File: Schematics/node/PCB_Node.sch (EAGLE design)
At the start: 19 parts, among them U1 ATMEGA328P, U2 MAX485CSA+, U3 MCP1824ST-3302E/DB

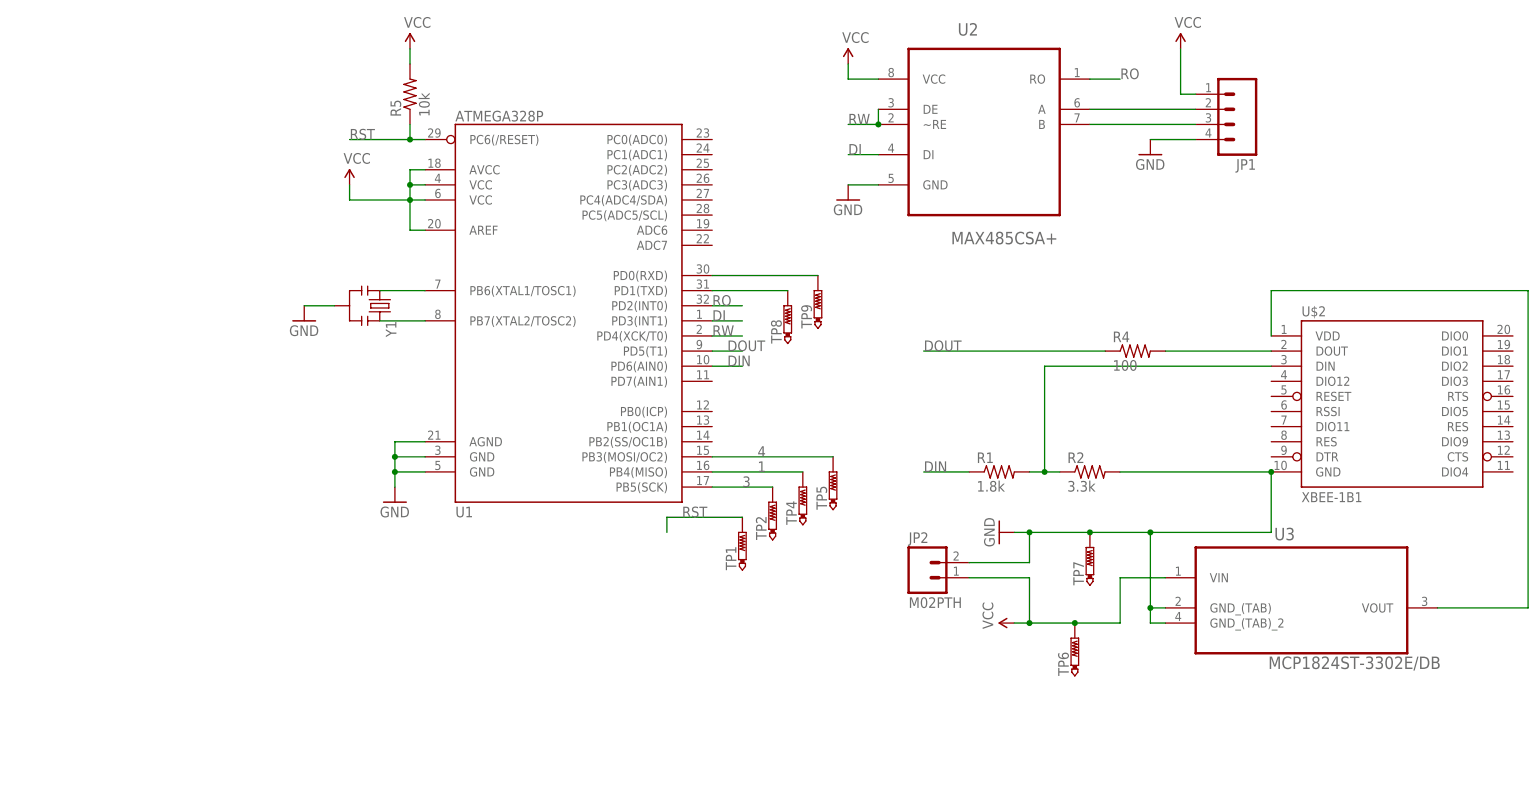
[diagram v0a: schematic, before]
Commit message: PCB updates
changed sensor PCB to 3.0
changed Node PCB to 2.0 and parts list to go with it (Sach, can you
look over the schematic, board, and parts list that I have so far to
make sure I have everything correct?)
added Base Station PCB 0.5
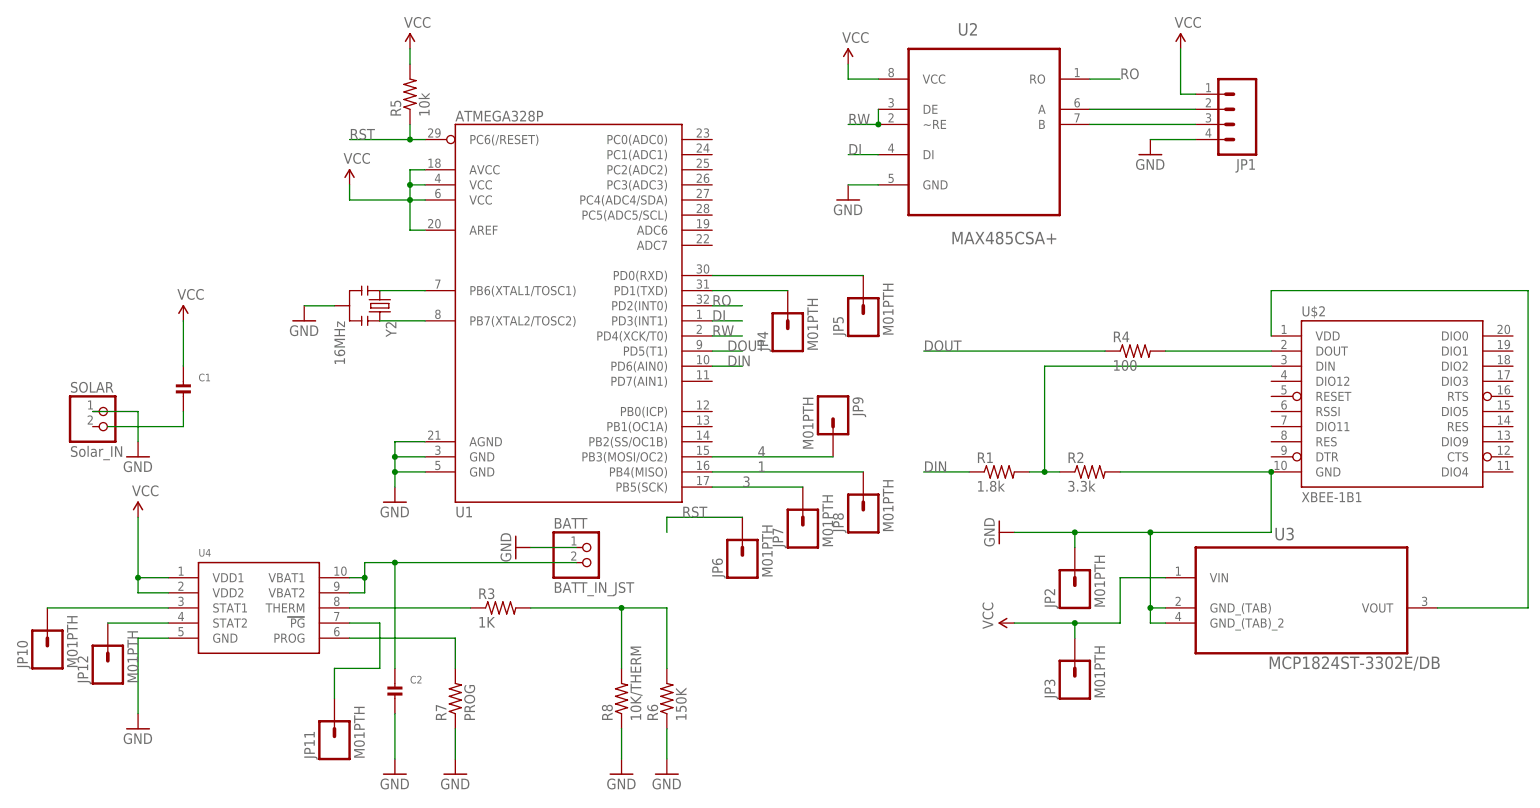
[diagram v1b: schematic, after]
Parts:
- removed TP1, TP2, TP4, TP5, TP6, TP7, TP8, TP9: PTR1TP12R, testpad:PTR1TP12R
- removed Y1: (no value), SparkFun-FreqCtrl:RESONATORPTH
- added BATT: BATT_IN_JST, microbuilder:JST_2PIN
- added C1, C2: (no value), microbuilder:CAP_CERAMIC0805
- added JP10, JP11, JP12, JP3, JP4, JP5, JP6, JP7, JP8, JP9: M01PTH, SparkFun-Connectors:M01PTH
- added R3: 1K, adafruit:R-US_R0805
- added R6: 150K, adafruit:R-US_R0805
- added R7: PROG, microbuilder:RESISTOR_DUAL
- added R8: 10K/THERM, adafruit:R-US_FLIPFLOP
- added SOLAR: Solar_IN, microbuilder:JST_2PIN
- added U4: (no value), microbuilder:MCP73833
- added Y2: 16MHz, SparkFun-FreqCtrl:RESONATOR16MHZ
- JP2: value M02PTH -> M01PTH; device SparkFun-Connectors:M02PTH -> SparkFun-Connectors:M01PTH
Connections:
- new net N$10: JP12.1, U4.STAT2
- new net N$11: JP11.1, U4.PG
- new net N$19: BATT.2, C2.P$1, U4.VBAT1, U4.VBAT2
- new net N$3: R7.2, U4.PROG
- new net N$5: R3.1, U4.THERM
- new net N$7: R3.2, R6.2, R8.2
- new net N$8: C1.P$2
- new net N$9: JP10.1, U4.STAT1
- net 1: now also JP8.1; no longer TP4.TP
- net 3: now also JP7.1; no longer TP2.TP
- net 4: now also JP9.1; no longer TP5.TP
- net GND: now also BATT.1, C2.P$2, JP2.1, R6.1, R7.1, R8.1, SOLAR.1, U4.GND, Y2.2; no longer JP2.2, TP7.TP, Y1.2
- net N$12: now also Y2.3; no longer Y1.3
- net N$13: now also Y2.1; no longer Y1.1
- net N$15: now also JP4.1; no longer TP8.TP
- net N$16: now also JP5.1; no longer TP9.TP
- net RST: now also JP6.1; no longer TP1.TP
- net VCC: now also C1.P$1, JP3.1, U4.VDD1, U4.VDD2; no longer JP2.1, TP6.TP

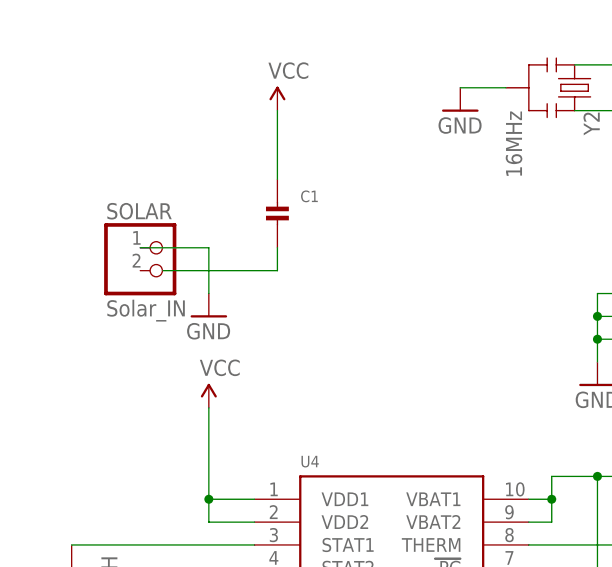
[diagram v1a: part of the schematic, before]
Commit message: Corrected Node PCB issues found by Sachleen for version 2.0
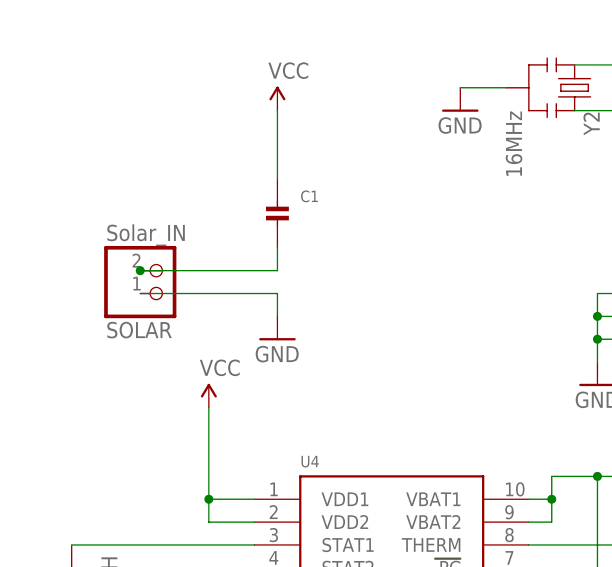
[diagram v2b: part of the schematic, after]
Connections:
- net N$8: now also SOLAR.2
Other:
- moved on the sheet: SOLAR
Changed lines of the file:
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@@
 <instance part="U4" gate="G$1" x="-144.78" y="25.4"/>
 <instance part="BATT" gate="G$1" x="-88.9" y="35.56"/>
-<instance part="SOLAR" gate="G$1" x="-170.18" y="58.42"/>
+<instance part="SOLAR" gate="G$1" x="-170.18" y="58.42" rot="MR180"/>
 <instance part="C1" gate="G$1" x="-157.48" y="63.5"/>
 <instance part="R3" gate="G$1" x="-104.14" y="27.94"/>
@@
 <instance part="GND10" gate="1" x="-76.2" y="0"/>
 <instance part="GND11" gate="1" x="-101.6" y="38.1" rot="R270"/>
-<instance part="GND12" gate="1" x="-165.1" y="53.34"/>
+<instance part="GND12" gate="1" x="-157.48" y="50.8"/>
 <instance part="SUPPLY7" gate="G$1" x="-157.48" y="76.2"/>
 <instance part="Y2" gate="G$1" x="-124.46" y="78.74" rot="R270"/>
@@
 </segment>
 <segment>
-<wire x1="-172.72" y1="60.96" x2="-165.1" y2="60.96" width="0.1524" layer="91"/>
+<wire x1="-172.72" y1="55.88" x2="-157.48" y2="55.88" width="0.1524" layer="91"/>
 <pinref part="SOLAR" gate="G$1" pin="1"/>
 <pinref part="GND12" gate="1" pin="GND"/>
-<wire x1="-165.1" y1="60.96" x2="-165.1" y2="55.88" width="0.1524" layer="91"/>
+<wire x1="-157.48" y1="55.88" x2="-157.48" y2="53.34" width="0.1524" layer="91"/>
 </segment>
 <segment>
@@
 <segment>
 <pinref part="C1" gate="G$1" pin="P$2"/>
-<wire x1="-170.18" y1="58.42" x2="-157.48" y2="58.42" width="0.1524" layer="91"/>
+<wire x1="-170.18" y1="58.42" x2="-172.72" y2="58.42" width="0.1524" layer="91"/>
+<wire x1="-172.72" y1="58.42" x2="-157.48" y2="58.42" width="0.1524" layer="91"/>
 <wire x1="-157.48" y1="58.42" x2="-157.48" y2="60.96" width="0.1524" layer="91"/>
-</segment>
-</net>
+<pinref part="SOLAR" gate="G$1" pin="2"/>
+<junction x="-172.72" y="58.42"/>
+</segment>
+</net>

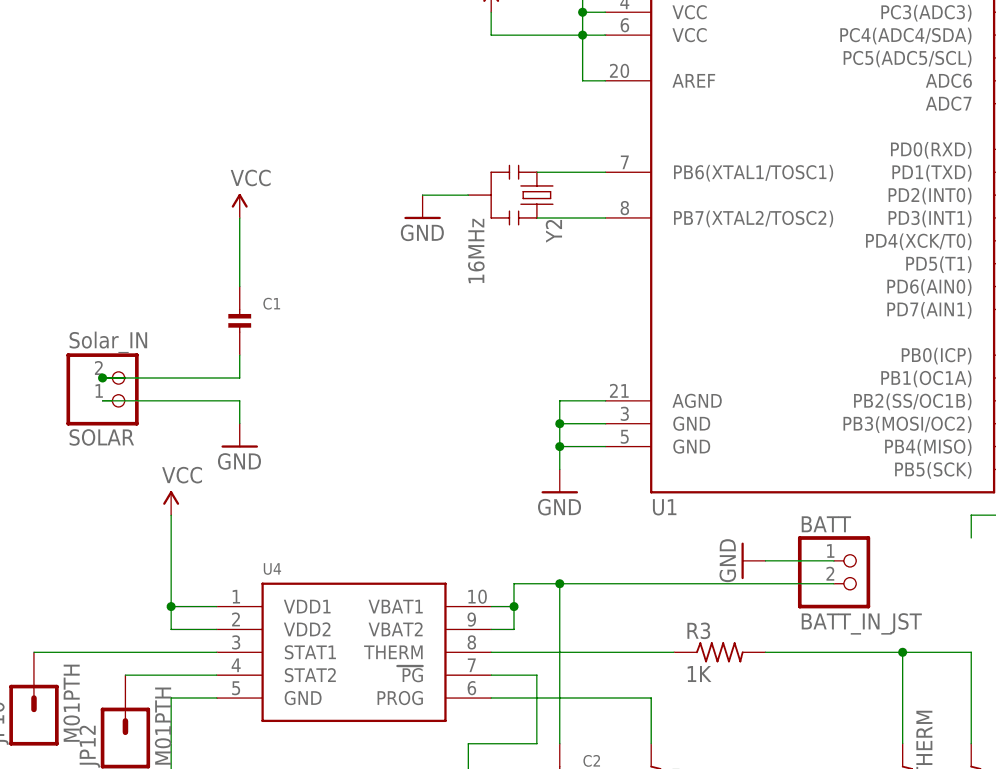
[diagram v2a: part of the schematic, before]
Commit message: Node Fixes
Made fixes to Node PCB.
- connected solar power to charging chip
- made power to battery and atmega from charging chip only
- rearranged board for these changes to work
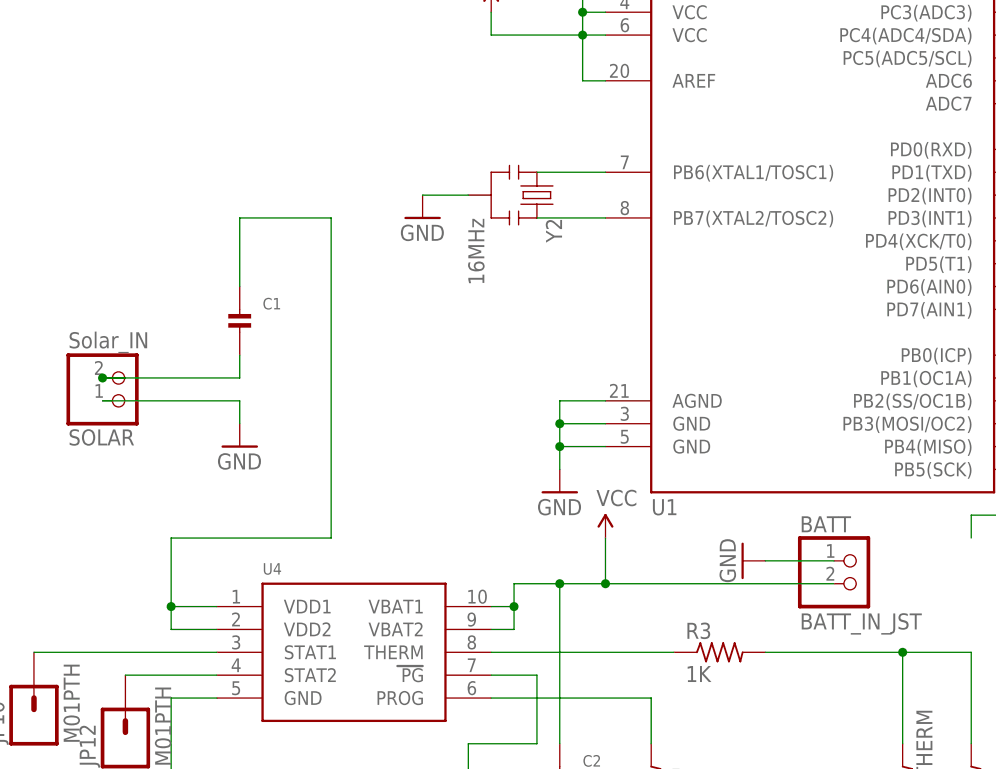
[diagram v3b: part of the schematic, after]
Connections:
- removed net N$19: BATT.2, C2.P$1, U4.VBAT1, U4.VBAT2
- new net N$14: C1.P$1, U4.VDD1, U4.VDD2
- net VCC: now also BATT.2, C2.P$1, U4.VBAT1, U4.VBAT2; no longer C1.P$1, U4.VDD1, U4.VDD2
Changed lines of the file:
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@@
 <part name="R6" library="adafruit" deviceset="R-US_" device="R0805" value="150K"/>
 <part name="R7" library="microbuilder" deviceset="RESISTOR_DUAL" device="" value="PROG"/>
-<part name="SUPPLY5" library="SparkFun-Aesthetics" deviceset="VCC" device=""/>
 <part name="GND6" library="SparkFun-Aesthetics" deviceset="GND" device=""/>
 <part name="R8" library="adafruit" deviceset="R-US_" device="FLIPFLOP" value="10K/THERM"/>
@@
 <part name="GND11" library="SparkFun-Aesthetics" deviceset="GND" device=""/>
 <part name="GND12" library="SparkFun-Aesthetics" deviceset="GND" device=""/>
-<part name="SUPPLY7" library="SparkFun-Aesthetics" deviceset="VCC" device=""/>
 <part name="Y2" library="SparkFun-FreqCtrl" deviceset="RESONATOR" device="16MHZ" value="16MHz"/>
 <part name="JP3" library="SparkFun-Connectors" deviceset="M01" device="PTH"/>
@@
 <part name="JP11" library="SparkFun-Connectors" deviceset="M01" device="PTH"/>
 <part name="JP12" library="SparkFun-Connectors" deviceset="M01" device="PTH"/>
+<part name="SUPPLY5" library="SparkFun-Aesthetics" deviceset="VCC" device=""/>
 </parts>
 <sheets>
@@
 <instance part="R6" gate="G$1" x="-76.2" y="12.7" rot="R90"/>
 <instance part="R7" gate="G$1" x="-111.76" y="12.7" rot="R90"/>
-<instance part="SUPPLY5" gate="G$1" x="-165.1" y="43.18"/>
 <instance part="GND6" gate="1" x="-165.1" y="7.62"/>
 <instance part="R8" gate="G$1" x="-83.82" y="12.7" rot="R90"/>
@@
 <instance part="GND11" gate="1" x="-101.6" y="38.1" rot="R270"/>
 <instance part="GND12" gate="1" x="-157.48" y="50.8"/>
-<instance part="SUPPLY7" gate="G$1" x="-157.48" y="76.2"/>
 <instance part="Y2" gate="G$1" x="-124.46" y="78.74" rot="R270"/>
 <instance part="JP3" gate="G$1" x="-7.62" y="15.24" rot="R90"/>
@@
 <instance part="JP11" gate="G$1" x="-132.08" y="5.08" rot="R90"/>
 <instance part="JP12" gate="G$1" x="-170.18" y="17.78" rot="R90"/>
+<instance part="SUPPLY5" gate="G$1" x="-116.84" y="40.64"/>
 </instances>
 <busses>
@@
 </segment>
 <segment>
-<pinref part="U4" gate="G$1" pin="VDD2"/>
-<pinref part="SUPPLY5" gate="G$1" pin="VCC"/>
-<wire x1="-160.02" y1="30.48" x2="-165.1" y2="30.48" width="0.1524" layer="91"/>
-<wire x1="-165.1" y1="30.48" x2="-165.1" y2="33.02" width="0.1524" layer="91"/>
-<pinref part="U4" gate="G$1" pin="VDD1"/>
-<wire x1="-165.1" y1="33.02" x2="-165.1" y2="43.18" width="0.1524" layer="91"/>
-<wire x1="-160.02" y1="33.02" x2="-165.1" y2="33.02" width="0.1524" layer="91"/>
-<junction x="-165.1" y="33.02"/>
-</segment>
-<segment>
-<pinref part="C1" gate="G$1" pin="P$1"/>
-<pinref part="SUPPLY7" gate="G$1" pin="VCC"/>
-<wire x1="-157.48" y1="68.58" x2="-157.48" y2="76.2" width="0.1524" layer="91"/>
-</segment>
-</net>
-<net name="N$3" class="0">
-<segment>
-<pinref part="U4" gate="G$1" pin="PROG"/>
-<pinref part="R7" gate="G$1" pin="2"/>
-<wire x1="-129.54" y1="22.86" x2="-111.76" y2="22.86" width="0.1524" layer="91"/>
-<wire x1="-111.76" y1="22.86" x2="-111.76" y2="17.78" width="0.1524" layer="91"/>
-</segment>
-</net>
-<net name="N$5" class="0">
-<segment>
-<pinref part="U4" gate="G$1" pin="THERM"/>
-<pinref part="R3" gate="G$1" pin="1"/>
-<wire x1="-129.54" y1="27.94" x2="-109.22" y2="27.94" width="0.1524" layer="91"/>
-</segment>
-</net>
-<net name="N$7" class="0">
-<segment>
-<pinref part="R3" gate="G$1" pin="2"/>
-<pinref part="R6" gate="G$1" pin="2"/>
-<wire x1="-99.06" y1="27.94" x2="-83.82" y2="27.94" width="0.1524" layer="91"/>
-<wire x1="-83.82" y1="27.94" x2="-76.2" y2="27.94" width="0.1524" layer="91"/>
-<wire x1="-76.2" y1="27.94" x2="-76.2" y2="17.78" width="0.1524" layer="91"/>
-<pinref part="R8" gate="G$1" pin="2"/>
-<wire x1="-83.82" y1="17.78" x2="-83.82" y2="27.94" width="0.1524" layer="91"/>
-<junction x="-83.82" y="27.94"/>
-</segment>
-</net>
-<net name="N$19" class="0">
-<segment>
 <pinref part="U4" gate="G$1" pin="VBAT1"/>
 <wire x1="-129.54" y1="33.02" x2="-127" y2="33.02" width="0.1524" layer="91"/>
@@
 <pinref part="C2" gate="G$1" pin="P$1"/>
 <wire x1="-121.92" y1="17.78" x2="-121.92" y2="35.56" width="0.1524" layer="91"/>
-<wire x1="-121.92" y1="35.56" x2="-91.44" y2="35.56" width="0.1524" layer="91"/>
+<wire x1="-121.92" y1="35.56" x2="-116.84" y2="35.56" width="0.1524" layer="91"/>
 <pinref part="BATT" gate="G$1" pin="2"/>
+<wire x1="-116.84" y1="35.56" x2="-91.44" y2="35.56" width="0.1524" layer="91"/>
 <wire x1="-127" y1="35.56" x2="-121.92" y2="35.56" width="0.1524" layer="91"/>
 <junction x="-121.92" y="35.56"/>
+<pinref part="SUPPLY5" gate="G$1" pin="VCC"/>
+<wire x1="-116.84" y1="40.64" x2="-116.84" y2="35.56" width="0.1524" layer="91"/>
+<junction x="-116.84" y="35.56"/>
+</segment>
+</net>
+<net name="N$3" class="0">
+<segment>
+<pinref part="U4" gate="G$1" pin="PROG"/>
+<pinref part="R7" gate="G$1" pin="2"/>
+<wire x1="-129.54" y1="22.86" x2="-111.76" y2="22.86" width="0.1524" layer="91"/>
+<wire x1="-111.76" y1="22.86" x2="-111.76" y2="17.78" width="0.1524" layer="91"/>
+</segment>
+</net>
+<net name="N$5" class="0">
+<segment>
+<pinref part="U4" gate="G$1" pin="THERM"/>
+<pinref part="R3" gate="G$1" pin="1"/>
+<wire x1="-129.54" y1="27.94" x2="-109.22" y2="27.94" width="0.1524" layer="91"/>
+</segment>
+</net>
+<net name="N$7" class="0">
+<segment>
+<pinref part="R3" gate="G$1" pin="2"/>
+<pinref part="R6" gate="G$1" pin="2"/>
+<wire x1="-99.06" y1="27.94" x2="-83.82" y2="27.94" width="0.1524" layer="91"/>
+<wire x1="-83.82" y1="27.94" x2="-76.2" y2="27.94" width="0.1524" layer="91"/>
+<wire x1="-76.2" y1="27.94" x2="-76.2" y2="17.78" width="0.1524" layer="91"/>
+<pinref part="R8" gate="G$1" pin="2"/>
+<wire x1="-83.82" y1="17.78" x2="-83.82" y2="27.94" width="0.1524" layer="91"/>
+<junction x="-83.82" y="27.94"/>
 </segment>
 </net>
@@
 </segment>
 </net>
+<net name="N$14" class="0">
+<segment>
+<pinref part="U4" gate="G$1" pin="VDD2"/>
+<wire x1="-160.02" y1="30.48" x2="-165.1" y2="30.48" width="0.1524" layer="91"/>
+<wire x1="-165.1" y1="30.48" x2="-165.1" y2="33.02" width="0.1524" layer="91"/>
+<pinref part="U4" gate="G$1" pin="VDD1"/>
+<wire x1="-165.1" y1="33.02" x2="-165.1" y2="40.64" width="0.1524" layer="91"/>
+<wire x1="-160.02" y1="33.02" x2="-165.1" y2="33.02" width="0.1524" layer="91"/>
+<junction x="-165.1" y="33.02"/>
+<pinref part="C1" gate="G$1" pin="P$1"/>
+<wire x1="-157.48" y1="68.58" x2="-157.48" y2="76.2" width="0.1524" layer="91"/>
+<wire x1="-157.48" y1="76.2" x2="-147.32" y2="76.2" width="0.1524" layer="91"/>
+<wire x1="-147.32" y1="76.2" x2="-147.32" y2="40.64" width="0.1524" layer="91"/>
+<wire x1="-147.32" y1="40.64" x2="-165.1" y2="40.64" width="0.1524" layer="91"/>
+</segment>
+</net>
